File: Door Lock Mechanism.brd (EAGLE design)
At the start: 68.6 x 53.3 mm, 4 parts

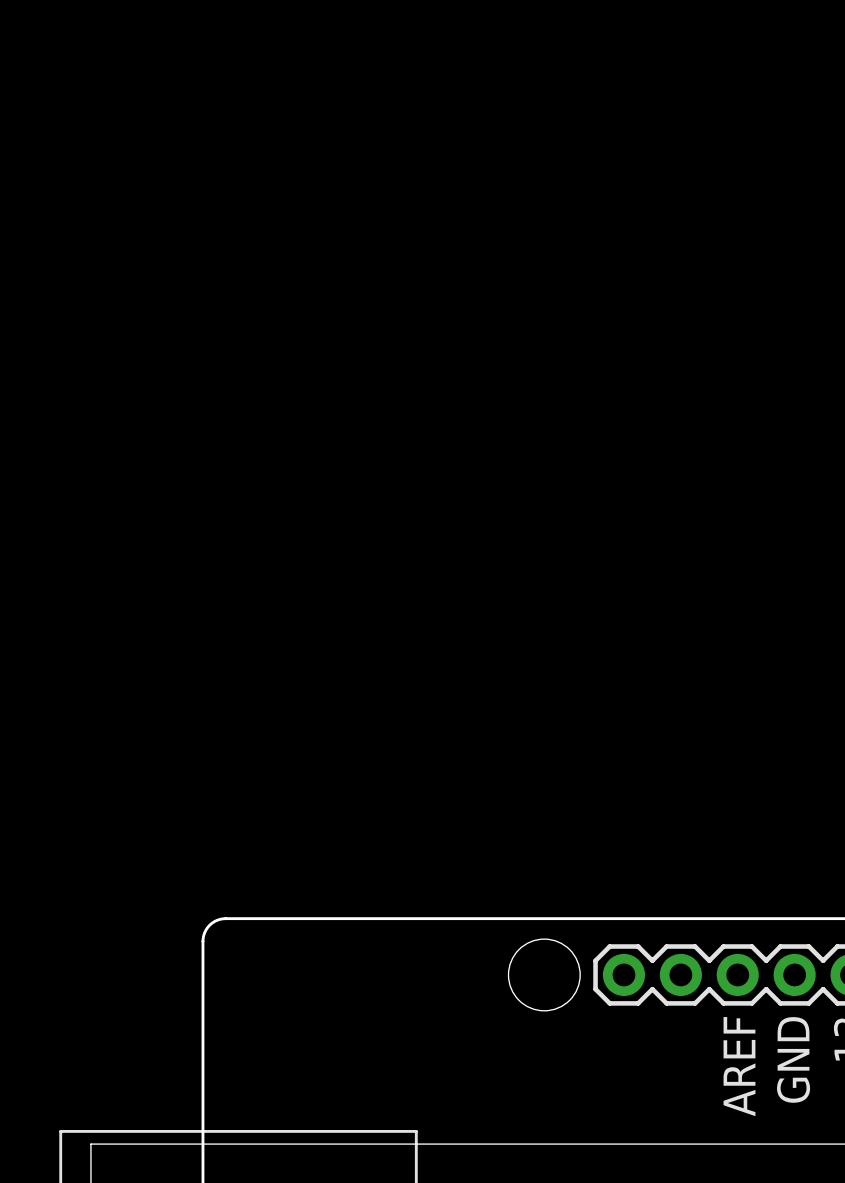
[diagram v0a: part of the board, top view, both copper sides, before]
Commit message: Update Door Lock Mechanism.brd
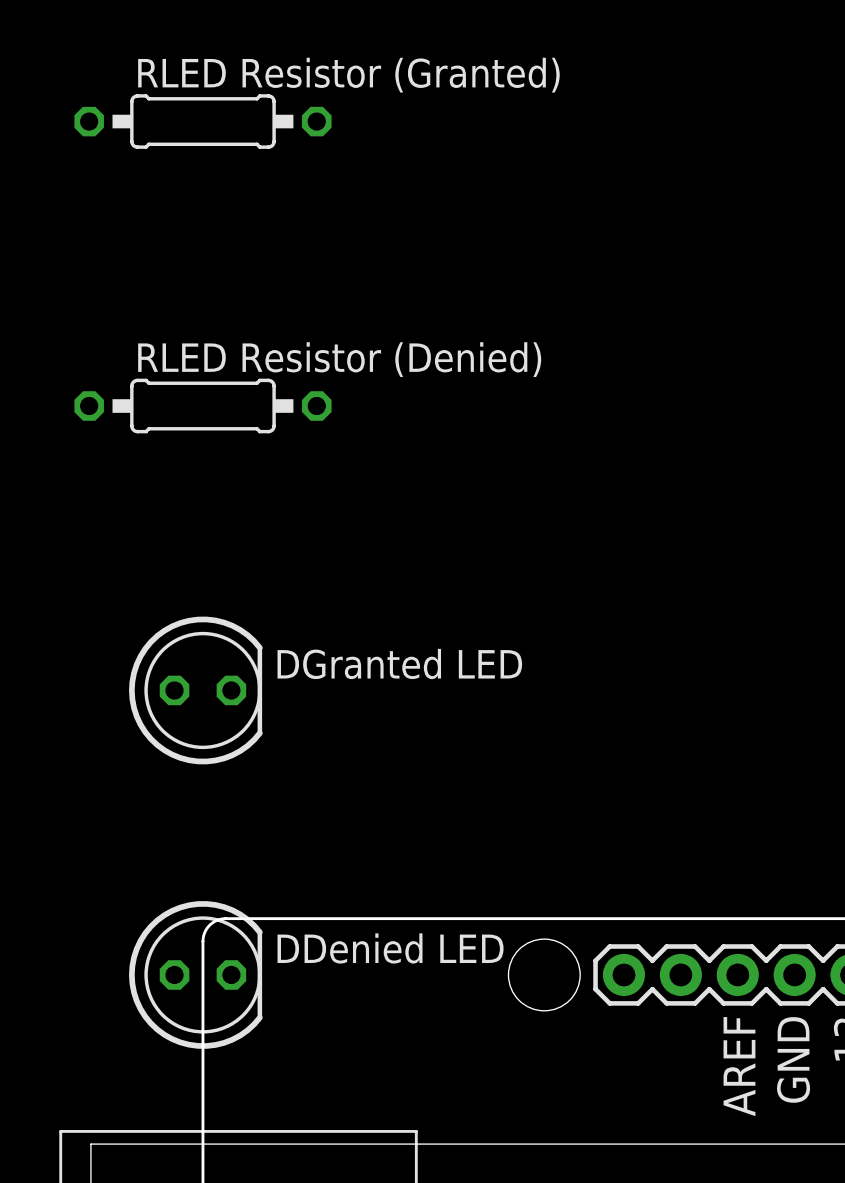
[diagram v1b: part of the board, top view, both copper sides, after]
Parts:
- added DDenied LED: (no value), AUTODESK_CIRCUITS_BREADBOARD:LED5MM
- added DGranted LED: (no value), AUTODESK_CIRCUITS_BREADBOARD:LED5MM
- added RLED Resistor (Denied): 0.45k‎Ω, AUTODESK_CIRCUITS_BREADBOARD:0207/10
- added RLED Resistor (Granted): 0.45k‎Ω, AUTODESK_CIRCUITS_BREADBOARD:0207/10
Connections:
- new net N$10: DGranted LED.A, RLED Resistor (Granted).2
- new net N$6: DDenied LED.K, DGranted LED.K, UArduino.GND
- new net N$7: RLED Resistor (Denied).1, UArduino.10
- new net N$8: DDenied LED.A, RLED Resistor (Denied).2
- new net N$9: RLED Resistor (Granted).1, UArduino.11
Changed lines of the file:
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@@
 </autorouter>
 <elements>
-<element value="" name="UArduino" library="AUTODESK_CIRCUITS_BREADBOARD" package="ARDUINO_UNO" x="5" y="10.08"></element><element value="" name="SERVOActuating Servo" library="AUTODESK_CIRCUITS_BREADBOARD" package="1X3P-2.54-2.54-11.6-3.0-BLACK-MALE" x="5" y="22.78"></element><element value="" name="SSwitch (Auth Standin)" library="AUTODESK_CIRCUITS_BREADBOARD" package="M251" x="5" y="35.480000000000004"></element><element value="1k‎Ω" name="RPull Down Resistor" library="AUTODESK_CIRCUITS_BREADBOARD" package="0207/10" x="5" y="48.18"></element></elements>
+<element value="" name="UArduino" library="AUTODESK_CIRCUITS_BREADBOARD" package="ARDUINO_UNO" x="5" y="10.08"></element><element value="" name="SERVOActuating Servo" library="AUTODESK_CIRCUITS_BREADBOARD" package="1X3P-2.54-2.54-11.6-3.0-BLACK-MALE" x="5" y="22.78"></element><element value="" name="SSwitch (Auth Standin)" library="AUTODESK_CIRCUITS_BREADBOARD" package="M251" x="5" y="35.480000000000004"></element><element value="1k‎Ω" name="RPull Down Resistor" library="AUTODESK_CIRCUITS_BREADBOARD" package="0207/10" x="5" y="48.18"></element><element value="" name="DDenied LED" library="AUTODESK_CIRCUITS_BREADBOARD" package="LED5MM" x="5" y="60.879999999999995"></element><element value="" name="DGranted LED" library="AUTODESK_CIRCUITS_BREADBOARD" package="LED5MM" x="5" y="73.58"></element><element value="0.45k‎Ω" name="RLED Resistor (Denied)" library="AUTODESK_CIRCUITS_BREADBOARD" package="0207/10" x="5" y="86.28"></element><element value="0.45k‎Ω" name="RLED Resistor (Granted)" library="AUTODESK_CIRCUITS_BREADBOARD" package="0207/10" x="5" y="98.98"></element></elements>
 <signals>
-<signal name="N$1"><contactref element="SERVOActuating Servo" pad="2"></contactref><contactref element="UArduino" pad="3.3V"></contactref><wire x1="5" y1="22.78" x2="40.56" y2="12.620000000000001" width="0" layer="19" extent="1-1"></wire></signal><signal name="N$2"><contactref element="SERVOActuating Servo" pad="1"></contactref><contactref element="UArduino" pad="GND.."></contactref><wire x1="5" y1="25.32" x2="45.64" y2="12.620000000000001" width="0" layer="19" extent="1-1"></wire><contactref element="RPull Down Resistor" pad="1"></contactref><wire x1="45.64" y1="12.620000000000001" x2="-0.08000000000000007" y2="48.18" width="0" layer="19" extent="1-1"></wire></signal><signal name="N$3"><contactref element="SERVOActuating Servo" pad="3"></contactref><contactref element="UArduino" pad="8"></contactref><wire x1="5" y1="20.240000000000002" x2="46.656" y2="60.879999999999995" width="0" layer="19" extent="1-1"></wire></signal><signal name="N$4"><contactref element="SSwitch (Auth Standin)" pad="3"></contactref><contactref element="UArduino" pad="9"></contactref><wire x1="7.54" y1="35.480000000000004" x2="44.116" y2="60.879999999999995" width="0" layer="19" extent="1-1"></wire><contactref element="RPull Down Resistor" pad="2"></contactref><wire x1="44.116" y1="60.879999999999995" x2="10.08" y2="48.18" width="0" layer="19" extent="1-1"></wire></signal><signal name="N$5"><contactref element="UArduino" pad="5V"></contactref><contactref element="SSwitch (Auth Standin)" pad="2"></contactref><wire x1="43.1" y1="12.620000000000001" x2="5" y2="35.480000000000004" width="0" layer="19" extent="1-1"></wire></signal></signals>
+<signal name="N$1"><contactref element="SERVOActuating Servo" pad="2"></contactref><contactref element="UArduino" pad="3.3V"></contactref><wire x1="5" y1="22.78" x2="40.56" y2="12.620000000000001" width="0" layer="19" extent="1-1"></wire></signal><signal name="N$2"><contactref element="SERVOActuating Servo" pad="1"></contactref><contactref element="UArduino" pad="GND.."></contactref><wire x1="5" y1="25.32" x2="45.64" y2="12.620000000000001" width="0" layer="19" extent="1-1"></wire><contactref element="RPull Down Resistor" pad="1"></contactref><wire x1="45.64" y1="12.620000000000001" x2="-0.08000000000000007" y2="48.18" width="0" layer="19" extent="1-1"></wire></signal><signal name="N$3"><contactref element="SERVOActuating Servo" pad="3"></contactref><contactref element="UArduino" pad="8"></contactref><wire x1="5" y1="20.240000000000002" x2="46.656" y2="60.879999999999995" width="0" layer="19" extent="1-1"></wire></signal><signal name="N$4"><contactref element="SSwitch (Auth Standin)" pad="3"></contactref><contactref element="UArduino" pad="9"></contactref><wire x1="7.54" y1="35.480000000000004" x2="44.116" y2="60.879999999999995" width="0" layer="19" extent="1-1"></wire><contactref element="RPull Down Resistor" pad="2"></contactref><wire x1="44.116" y1="60.879999999999995" x2="10.08" y2="48.18" width="0" layer="19" extent="1-1"></wire></signal><signal name="N$5"><contactref element="UArduino" pad="5V"></contactref><contactref element="SSwitch (Auth Standin)" pad="2"></contactref><wire x1="43.1" y1="12.620000000000001" x2="5" y2="35.480000000000004" width="0" layer="19" extent="1-1"></wire></signal><signal name="N$6"><contactref element="UArduino" pad="GND"></contactref><contactref element="DDenied LED" pad="K"></contactref><wire x1="31.416" y1="60.879999999999995" x2="6.27" y2="60.879999999999995" width="0" layer="19" extent="1-1"></wire><contactref element="DGranted LED" pad="K"></contactref><wire x1="6.27" y1="60.879999999999995" x2="6.27" y2="73.58" width="0" layer="19" extent="1-1"></wire></signal><signal name="N$7"><contactref element="UArduino" pad="10"></contactref><contactref element="RLED Resistor (Denied)" pad="1"></contactref><wire x1="41.576" y1="60.879999999999995" x2="-0.08000000000000007" y2="86.28" width="0" layer="19" extent="1-1"></wire></signal><signal name="N$8"><contactref element="RLED Resistor (Denied)" pad="2"></contactref><contactref element="DDenied LED" pad="A"></contactref><wire x1="10.08" y1="86.28" x2="3.73" y2="60.879999999999995" width="0" layer="19" extent="1-1"></wire></signal><signal name="N$9"><contactref element="UArduino" pad="11"></contactref><contactref element="RLED Resistor (Granted)" pad="1"></contactref><wire x1="39.036" y1="60.879999999999995" x2="-0.08000000000000007" y2="98.98" width="0" layer="19" extent="1-1"></wire></signal><signal name="N$10"><contactref element="RLED Resistor (Granted)" pad="2"></contactref><contactref element="DGranted LED" pad="A"></contactref><wire x1="10.08" y1="98.98" x2="3.73" y2="73.58" width="0" layer="19" extent="1-1"></wire></signal></signals>
 </board>
 </drawing>
